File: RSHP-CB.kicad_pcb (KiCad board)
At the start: 2 copper layers, 140 x 120 mm, 23 parts, among them J1 Conn_02x20_Odd_Even, J2 Conn_02x02_Odd_Even, J3 Conn_02x02_Odd_Even, J4 Conn_02x04_Odd_Even

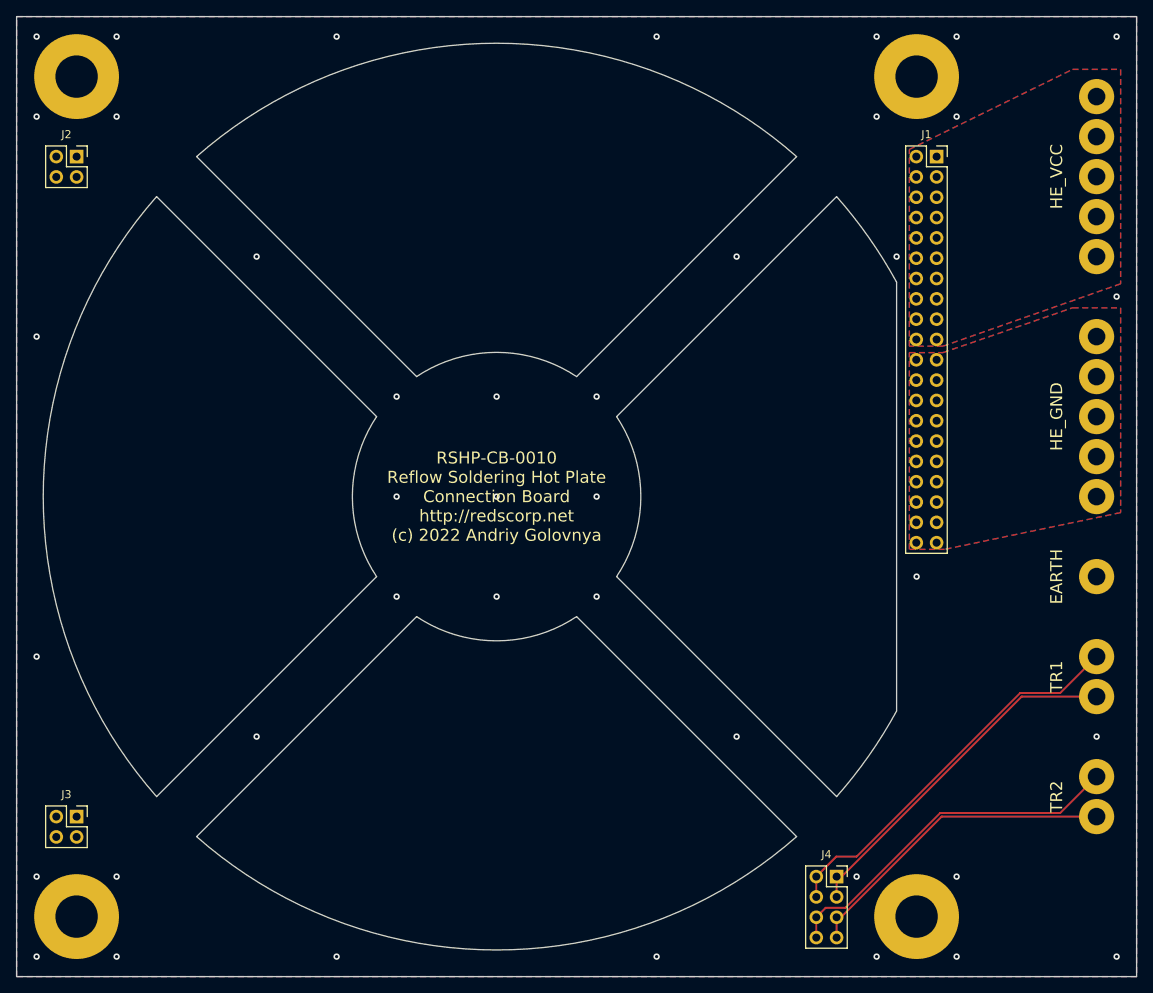
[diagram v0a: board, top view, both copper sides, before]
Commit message: Changed mount holes to M4 diameter. Generated CAM files.
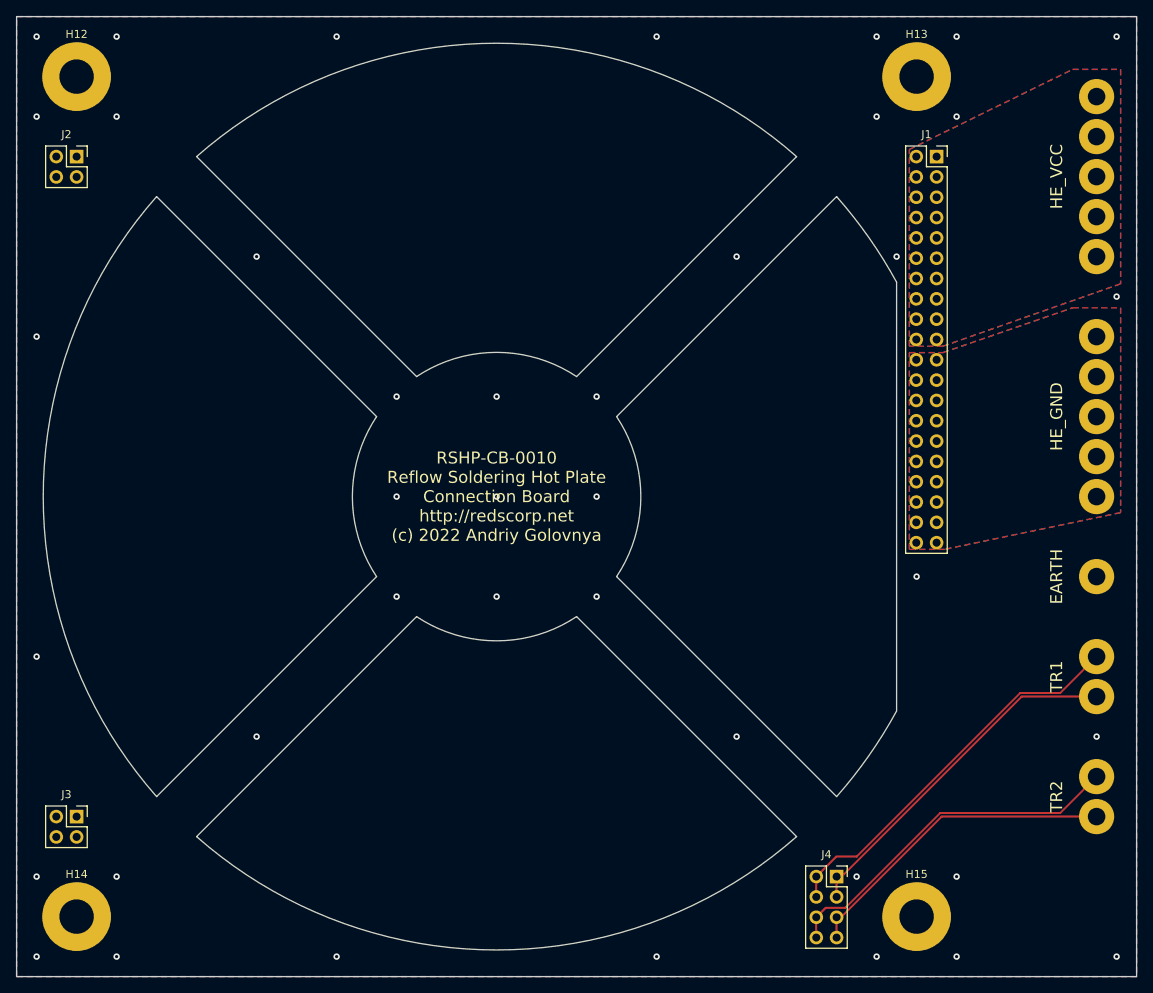
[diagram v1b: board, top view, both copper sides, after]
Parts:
- H12, H13, H14, H15: footprint MountingHole:MountingHole_5.3mm_M5_Pad -> MountingHole:MountingHole_4.3mm_M4_Pad
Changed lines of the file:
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@@
   (title_block
     (title "RSHP-CB-0010")
-    (date "2022-05-21")
+    (date "2022-05-25")
     (rev "1.0")
     (company "(c) Andriy Golovnya http://redscorp.net")
@@
       (net 2 "HE_GND") (pinfunction "1") (pintype "input"))
   )
-  (footprint "MountingHole:MountingHole_5.3mm_M5_Pad" (layer "F.Cu")
+  (footprint "MountingHole:MountingHole_4.3mm_M4_Pad" (layer "F.Cu")
     (at 57.5 142.5)
-    (descr "Mounting Hole 5.3mm, M5")
-    (tags "mounting hole 5.3mm m5")
-    (property "Sheetfile" "RSHP-CB.kicad_sch")
-    (property "Sheetname" "")
-    (attr exclude_from_pos_files)
-    (fp_text reference "H14" (at 0 -6.3) (layer "F.SilkS") hide
-      (effects (font (size 1 1) (thickness 0.15)))
-    )
-    (fp_text value "MountingHole" (at 0 6.3) (layer "F.Fab")
-      (effects (font (size 1 1) (thickness 0.15)))
-    )
-    (fp_text user "${REFERENCE}" (at 0 0) (layer "F.Fab")
-      (effects (font (size 1 1) (thickness 0.15)))
-    )
-    (fp_circle (center 0 0) (end 5.3 0) (layer "Cmts.User") (width 0.15) (fill none))
-    (fp_circle (center 0 0) (end 5.55 0) (layer "F.CrtYd") (width 0.05) (fill none))
-    (pad "1" thru_hole circle (at 0 0) (size 10.6 10.6) (drill 5.3) (layers *.Cu *.Mask)
+    (descr "Mounting Hole 4.3mm, M4")
+    (tags "mounting hole 4.3mm m4")
+    (property "Sheetfile" "RSHP-CB.kicad_sch")
+    (property "Sheetname" "")
+    (attr exclude_from_pos_files)
+    (fp_text reference "H14" (at 0 -5.3) (layer "F.SilkS")
+      (effects (font (size 1 1) (thickness 0.15)))
+    )
+    (fp_text value "MountingHole" (at 0 5.3) (layer "F.Fab")
+      (effects (font (size 1 1) (thickness 0.15)))
+    )
+    (fp_text user "${REFERENCE}" (at 0 0) (layer "F.Fab")
+      (effects (font (size 1 1) (thickness 0.15)))
+    )
+    (fp_circle (center 0 0) (end 4.3 0) (layer "Cmts.User") (width 0.15) (fill none))
+    (fp_circle (center 0 0) (end 4.55 0) (layer "F.CrtYd") (width 0.05) (fill none))
+    (pad "1" thru_hole circle (at 0 0) (size 8.6 8.6) (drill 4.3) (layers *.Cu *.Mask)
       (net 3 "EARTH") (pinfunction "1") (pintype "input"))
   )
@@
       (net 2 "HE_GND") (pinfunction "1") (pintype "input"))
   )
-  (footprint "MountingHole:MountingHole_5.3mm_M5_Pad" (layer "F.Cu")
+  (footprint "MountingHole:MountingHole_4.3mm_M4_Pad" (layer "F.Cu")
     (at 57.5 37.5)
-    (descr "Mounting Hole 5.3mm, M5")
-    (tags "mounting hole 5.3mm m5")
-    (property "Sheetfile" "RSHP-CB.kicad_sch")
-    (property "Sheetname" "")
-    (attr exclude_from_pos_files)
-    (fp_text reference "H12" (at 0 -6.3) (layer "F.SilkS") hide
-      (effects (font (size 1 1) (thickness 0.15)))
-    )
-    (fp_text value "MountingHole" (at 0 6.3) (layer "F.Fab")
-      (effects (font (size 1 1) (thickness 0.15)))
-    )
-    (fp_text user "${REFERENCE}" (at 0 0) (layer "F.Fab")
-      (effects (font (size 1 1) (thickness 0.15)))
-    )
-    (fp_circle (center 0 0) (end 5.3 0) (layer "Cmts.User") (width 0.15) (fill none))
-    (fp_circle (center 0 0) (end 5.55 0) (layer "F.CrtYd") (width 0.05) (fill none))
-    (pad "1" thru_hole circle (at 0 0) (size 10.6 10.6) (drill 5.3) (layers *.Cu *.Mask)
+    (descr "Mounting Hole 4.3mm, M4")
+    (tags "mounting hole 4.3mm m4")
+    (property "Sheetfile" "RSHP-CB.kicad_sch")
+    (property "Sheetname" "")
+    (attr exclude_from_pos_files)
+    (fp_text reference "H12" (at 0 -5.3) (layer "F.SilkS")
+      (effects (font (size 1 1) (thickness 0.15)))
+    )
+    (fp_text value "MountingHole" (at 0 5.3) (layer "F.Fab")
+      (effects (font (size 1 1) (thickness 0.15)))
+    )
+    (fp_text user "${REFERENCE}" (at 0 0) (layer "F.Fab")
+      (effects (font (size 1 1) (thickness 0.15)))
+    )
+    (fp_circle (center 0 0) (end 4.3 0) (layer "Cmts.User") (width 0.15) (fill none))
+    (fp_circle (center 0 0) (end 4.55 0) (layer "F.CrtYd") (width 0.05) (fill none))
+    (pad "1" thru_hole circle (at 0 0) (size 8.6 8.6) (drill 4.3) (layers *.Cu *.Mask)
       (net 3 "EARTH") (pinfunction "1") (pintype "input"))
   )
-  (footprint "MountingHole:MountingHole_5.3mm_M5_Pad" (layer "F.Cu")
+  (footprint "MountingHole:MountingHole_4.3mm_M4_Pad" (layer "F.Cu")
     (at 162.5 142.5)
-    (descr "Mounting Hole 5.3mm, M5")
-    (tags "mounting hole 5.3mm m5")
-    (property "Sheetfile" "RSHP-CB.kicad_sch")
-    (property "Sheetname" "")
-    (attr exclude_from_pos_files)
-    (fp_text reference "H15" (at 0 -6.3) (layer "F.SilkS") hide
-      (effects (font (size 1 1) (thickness 0.15)))
-    )
-    (fp_text value "MountingHole" (at 0 6.3) (layer "F.Fab")
-      (effects (font (size 1 1) (thickness 0.15)))
-    )
-    (fp_text user "${REFERENCE}" (at 0 0) (layer "F.Fab")
-      (effects (font (size 1 1) (thickness 0.15)))
-    )
-    (fp_circle (center 0 0) (end 5.3 0) (layer "Cmts.User") (width 0.15) (fill none))
-    (fp_circle (center 0 0) (end 5.55 0) (layer "F.CrtYd") (width 0.05) (fill none))
-    (pad "1" thru_hole circle (at 0 0) (size 10.6 10.6) (drill 5.3) (layers *.Cu *.Mask)
+    (descr "Mounting Hole 4.3mm, M4")
+    (tags "mounting hole 4.3mm m4")
+    (property "Sheetfile" "RSHP-CB.kicad_sch")
+    (property "Sheetname" "")
+    (attr exclude_from_pos_files)
+    (fp_text reference "H15" (at 0 -5.3) (layer "F.SilkS")
+      (effects (font (size 1 1) (thickness 0.15)))
+    )
+    (fp_text value "MountingHole" (at 0 5.3) (layer "F.Fab")
+      (effects (font (size 1 1) (thickness 0.15)))
+    )
+    (fp_text user "${REFERENCE}" (at 0 0) (layer "F.Fab")
+      (effects (font (size 1 1) (thickness 0.15)))
+    )
+    (fp_circle (center 0 0) (end 4.3 0) (layer "Cmts.User") (width 0.15) (fill none))
+    (fp_circle (center 0 0) (end 4.55 0) (layer "F.CrtYd") (width 0.05) (fill none))
+    (pad "1" thru_hole circle (at 0 0) (size 8.6 8.6) (drill 4.3) (layers *.Cu *.Mask)
       (net 3 "EARTH") (pinfunction "1") (pintype "input"))
   )
@@
       (net 2 "HE_GND") (pinfunction "1") (pintype "input"))
   )
-  (footprint "MountingHole:MountingHole_5.3mm_M5_Pad" (layer "F.Cu")
+  (footprint "MountingHole:MountingHole_4.3mm_M4_Pad" (layer "F.Cu")
     (at 162.5 37.5)
-    (descr "Mounting Hole 5.3mm, M5")
-    (tags "mounting hole 5.3mm m5")
-    (property "Sheetfile" "RSHP-CB.kicad_sch")
-    (property "Sheetname" "")
-    (attr exclude_from_pos_files)
-    (fp_text reference "H13" (at 0 -6.3) (layer "F.SilkS") hide
-      (effects (font (size 1 1) (thickness 0.15)))
-    )
-    (fp_text value "MountingHole" (at 0 6.3) (layer "F.Fab")
-      (effects (font (size 1 1) (thickness 0.15)))
-    )
-    (fp_text user "${REFERENCE}" (at 0 0) (layer "F.Fab")
-      (effects (font (size 1 1) (thickness 0.15)))
-    )
-    (fp_circle (center 0 0) (end 5.3 0) (layer "Cmts.User") (width 0.15) (fill none))
-    (fp_circle (center 0 0) (end 5.55 0) (layer "F.CrtYd") (width 0.05) (fill none))
-    (pad "1" thru_hole circle (at 0 0) (size 10.6 10.6) (drill 5.3) (layers *.Cu *.Mask)
+    (descr "Mounting Hole 4.3mm, M4")
+    (tags "mounting hole 4.3mm m4")
+    (property "Sheetfile" "RSHP-CB.kicad_sch")
+    (property "Sheetname" "")
+    (attr exclude_from_pos_files)
+    (fp_text reference "H13" (at 0 -5.3) (layer "F.SilkS")
+      (effects (font (size 1 1) (thickness 0.15)))
+    )
+    (fp_text value "MountingHole" (at 0 5.3) (layer "F.Fab")
+      (effects (font (size 1 1) (thickness 0.15)))
+    )
+    (fp_text user "${REFERENCE}" (at 0 0) (layer "F.Fab")
+      (effects (font (size 1 1) (thickness 0.15)))
+    )
+    (fp_circle (center 0 0) (end 4.3 0) (layer "Cmts.User") (width 0.15) (fill none))
+    (fp_circle (center 0 0) (end 4.55 0) (layer "F.CrtYd") (width 0.05) (fill none))
+    (pad "1" thru_hole circle (at 0 0) (size 8.6 8.6) (drill 4.3) (layers *.Cu *.Mask)
       (net 3 "EARTH") (pinfunction "1") (pintype "input"))
   )

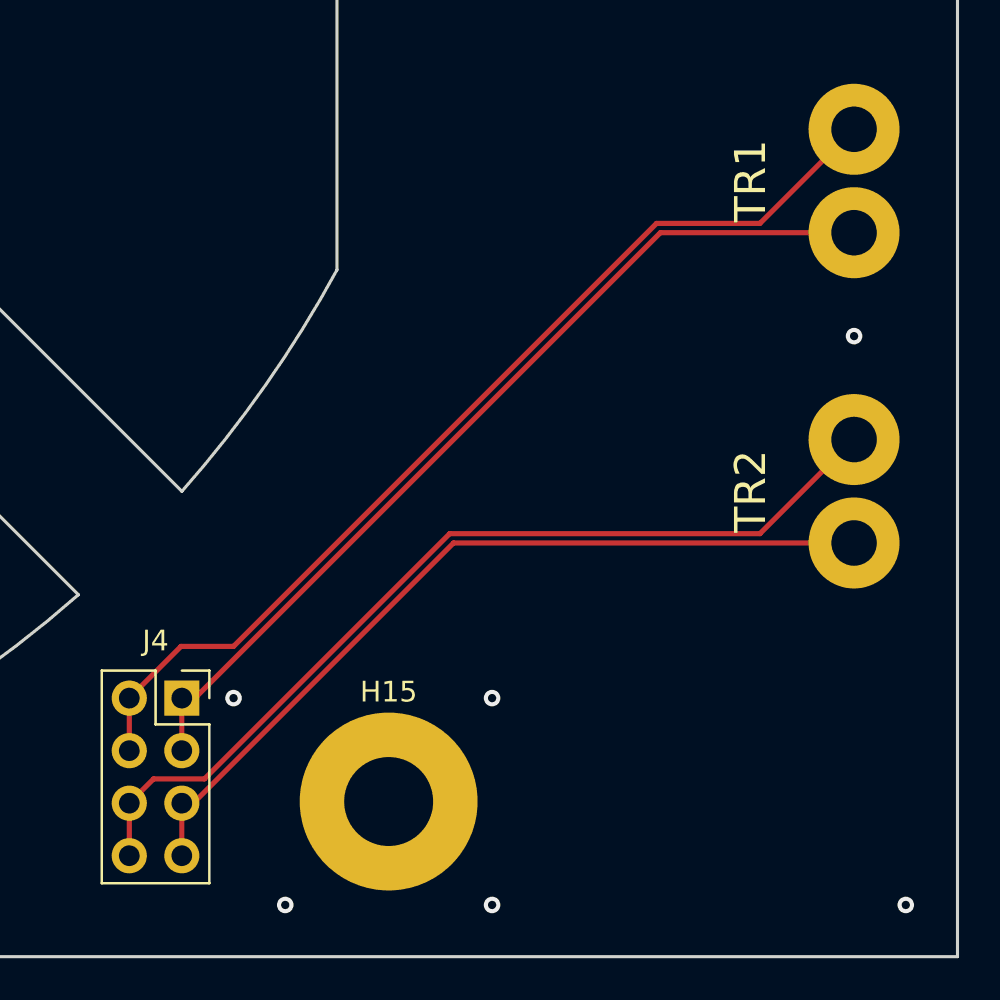
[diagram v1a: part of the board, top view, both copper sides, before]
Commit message: Made TR1 and TR2 wires thicker. Generated CAM files. Generated PNG preview.
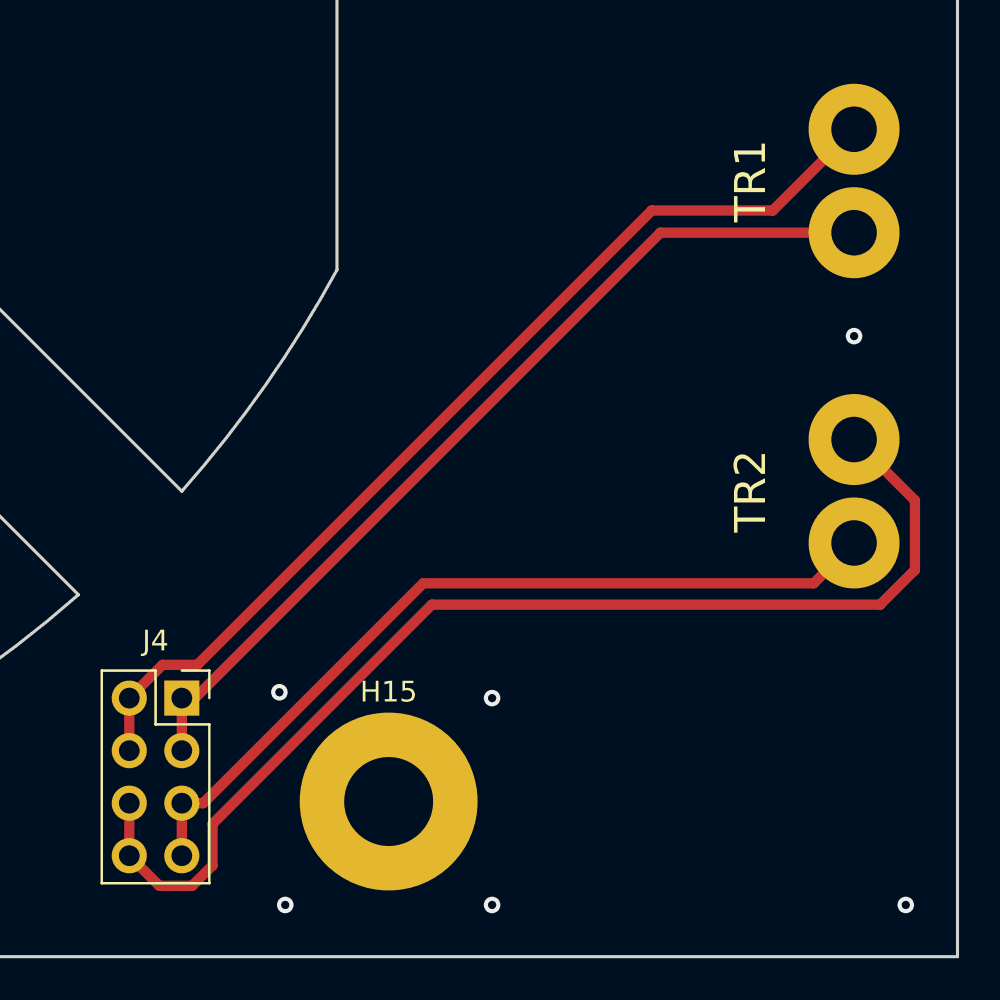
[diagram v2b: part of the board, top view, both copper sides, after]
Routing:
- net TR2_VCC: track 44.9 -> 56.1 mm
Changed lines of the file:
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@@
   (title_block
     (title "RSHP-CB-0010")
-    (date "2022-05-25")
+    (date "2022-05-29")
     (rev "1.0")
     (company "(c) Andriy Golovnya http://redscorp.net")
@@
   (gr_arc (start 100 75) (mid 110 71.971297) (end 120 75) (layer "Edge.Cuts") (width 0.15))
   (gr_line (start 95 80) (end 67.5 52.5) (layer "Edge.Cuts") (width 0.15))
-  (gr_arc (start 160 116.8) (mid 156.55161 122.361573) (end 152.503633 127.503205) (layer "Edge.Cuts") (width 0.15))
+  (gr_arc (start 160 116.8) (mid 156.55069 122.360764) (end 152.5 127.5) (layer "Edge.Cuts") (width 0.15))
   (gr_arc (start 95 100) (mid 91.971297 90) (end 95 80) (layer "Edge.Cuts") (width 0.15))
   (gr_line (start 50 30) (end 170 150) (layer "User.1") (width 0.15))
@@
   (via (at 97.5 77.5) (size 0.8) (drill 0.4) (layers "F.Cu" "B.Cu") (free) (net 3))
   (via (at 122.5 90) (size 0.8) (drill 0.4) (layers "F.Cu" "B.Cu") (free) (net 3))
-  (via (at 155 137.5) (size 0.8) (drill 0.4) (layers "F.Cu" "B.Cu") (free) (net 3))
+  (via (at 157.217171 137.217171) (size 0.8) (drill 0.4) (layers "F.Cu" "B.Cu") (free) (net 3))
   (via (at 157.5 32.5) (size 0.8) (drill 0.4) (layers "F.Cu" "B.Cu") (free) (net 3))
   (via (at 187.5 147.5) (size 0.8) (drill 0.4) (layers "F.Cu" "B.Cu") (free) (net 3))
@@
   (via (at 52.5 147.5) (size 0.8) (drill 0.4) (layers "F.Cu" "B.Cu") (free) (net 3))
   (via (at 140 60) (size 0.8) (drill 0.4) (layers "F.Cu" "B.Cu") (free) (net 3))
-  (segment (start 152.46 135) (end 155.000001 135) (width 0.25) (layer "F.Cu") (net 4))
-  (segment (start 149.96 140.04) (end 149.96 137.5) (width 0.25) (layer "F.Cu") (net 4))
-  (segment (start 180.44952 114.55048) (end 185 110) (width 0.25) (layer "F.Cu") (net 4))
-  (segment (start 155.000001 135) (end 175.449521 114.55048) (width 0.25) (layer "F.Cu") (net 4))
-  (segment (start 175.449521 114.55048) (end 180.44952 114.55048) (width 0.25) (layer "F.Cu") (net 4))
-  (segment (start 149.96 137.5) (end 152.46 135) (width 0.25) (layer "F.Cu") (net 4))
-  (segment (start 152.5 140.04) (end 152.5 137.5) (width 0.25) (layer "F.Cu") (net 5))
-  (segment (start 153.135718 137.5) (end 175.635718 115) (width 0.25) (layer "F.Cu") (net 5))
-  (segment (start 175.635718 115) (end 185 115) (width 0.25) (layer "F.Cu") (net 5))
-  (segment (start 152.5 137.5) (end 153.135718 137.5) (width 0.25) (layer "F.Cu") (net 5))
-  (segment (start 153.594511 141.405489) (end 165.449521 129.55048) (width 0.25) (layer "F.Cu") (net 6))
-  (segment (start 165.449521 129.55048) (end 180.44952 129.55048) (width 0.25) (layer "F.Cu") (net 6))
-  (segment (start 149.96 145.12) (end 149.96 142.58) (width 0.25) (layer "F.Cu") (net 6))
-  (segment (start 149.96 142.58) (end 151.134511 141.405489) (width 0.25) (layer "F.Cu") (net 6))
-  (segment (start 180.44952 129.55048) (end 185 125) (width 0.25) (layer "F.Cu") (net 6))
-  (segment (start 151.134511 141.405489) (end 153.594511 141.405489) (width 0.25) (layer "F.Cu") (net 6))
-  (segment (start 153.055718 142.58) (end 165.635718 130) (width 0.25) (layer "F.Cu") (net 7))
-  (segment (start 152.5 142.58) (end 153.055718 142.58) (width 0.25) (layer "F.Cu") (net 7))
-  (segment (start 152.5 145.12) (end 152.5 142.58) (width 0.25) (layer "F.Cu") (net 7))
-  (segment (start 165.635718 130) (end 185 130) (width 0.25) (layer "F.Cu") (net 7))
+  (segment (start 149.96 140.04) (end 149.96 137.5) (width 0.5) (layer "F.Cu") (net 4))
+  (segment (start 149.96 137.5) (end 151.570201 135.889799) (width 0.5) (layer "F.Cu") (net 4))
+  (segment (start 181.072526 113.927474) (end 185 110) (width 0.5) (layer "F.Cu") (net 4))
+  (segment (start 175.214504 113.927474) (end 181.072526 113.927474) (width 0.5) (layer "F.Cu") (net 4))
+  (segment (start 153.252179 135.889799) (end 175.214504 113.927474) (width 0.5) (layer "F.Cu") (net 4))
+  (segment (start 151.570201 135.889799) (end 153.252179 135.889799) (width 0.5) (layer "F.Cu") (net 4))
+  (segment (start 152.5 140.04) (end 152.5 137.5) (width 0.5) (layer "F.Cu") (net 5))
+  (segment (start 153.135718 137.5) (end 175.635718 115) (width 0.5) (layer "F.Cu") (net 5))
+  (segment (start 175.635718 115) (end 185 115) (width 0.5) (layer "F.Cu") (net 5))
+  (segment (start 152.5 137.5) (end 153.135718 137.5) (width 0.5) (layer "F.Cu") (net 5))
+  (segment (start 187.941812 127.941812) (end 185 125) (width 0.5) (layer "F.Cu") (net 6))
+  (segment (start 164.586304 132.982636) (end 186.261522 132.982636) (width 0.5) (layer "F.Cu") (net 6))
+  (segment (start 149.96 145.12) (end 149.96 142.58) (width 0.5) (layer "F.Cu") (net 6))
+  (segment (start 149.96 145.12) (end 151.415598 146.575598) (width 0.5) (layer "F.Cu") (net 6))
+  (segment (start 153.983086 143.585854) (end 164.586304 132.982636) (width 0.5) (layer "F.Cu") (net 6))
+  (segment (start 153.983086 145.590463) (end 153.983086 143.585854) (width 0.5) (layer "F.Cu") (net 6))
+  (segment (start 151.415598 146.575598) (end 152.997951 146.575598) (width 0.5) (layer "F.Cu") (net 6))
+  (segment (start 186.261522 132.982636) (end 187.941812 131.302346) (width 0.5) (layer "F.Cu") (net 6))
+  (segment (start 152.997951 146.575598) (end 153.983086 145.590463) (width 0.5) (layer "F.Cu") (net 6))
+  (segment (start 187.941812 131.302346) (end 187.941812 127.941812) (width 0.5) (layer "F.Cu") (net 6))
+  (segment (start 164.165081 131.949991) (end 183.050009 131.949991) (width 0.5) (layer "F.Cu") (net 7))
+  (segment (start 152.5 142.58) (end 153.535072 142.58) (width 0.5) (layer "F.Cu") (net 7))
+  (segment (start 183.050009 131.949991) (end 185 130) (width 0.5) (layer "F.Cu") (net 7))
+  (segment (start 152.5 145.12) (end 152.5 142.58) (width 0.5) (layer "F.Cu") (net 7))
+  (segment (start 153.535072 142.58) (end 164.165081 131.949991) (width 0.5) (layer "F.Cu") (net 7))
   (zone (net 2) (net_name "HE_GND") (layers F&B.Cu) (hatch edge 0.508)
     (priority 1)
